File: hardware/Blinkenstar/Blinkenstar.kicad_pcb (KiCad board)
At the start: 2 copper layers, 84.4 x 82.8 mm, 21 parts, among them J1 AudioJack2_Ground, U2 ATtiny88-A, U3 EEPROM-I2CEIAJ

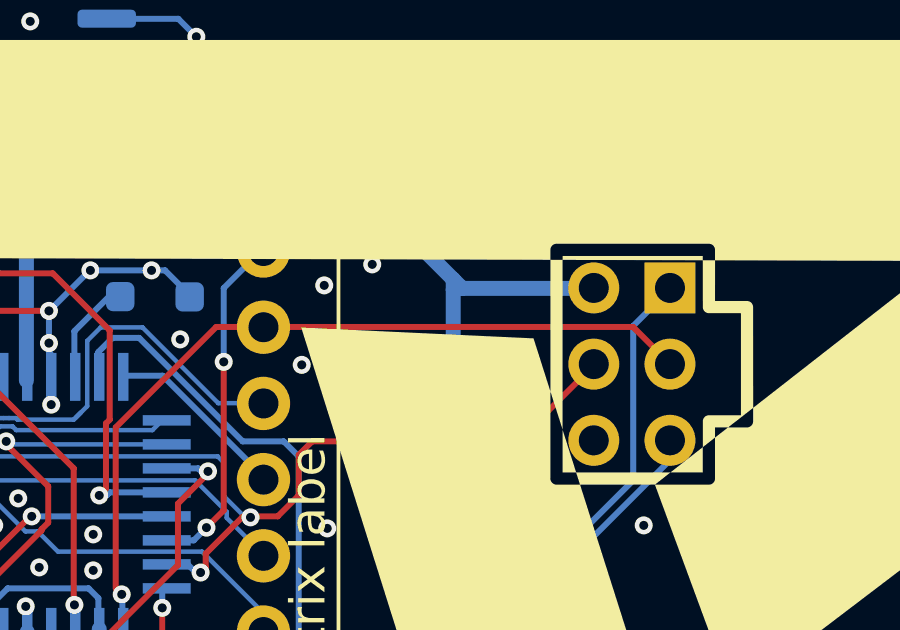
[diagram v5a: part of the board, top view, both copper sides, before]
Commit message: Adds CLKI connector for clock input
Adds a single-pin connector for external clock input (CLKI).

This enables the Blinkenstar to synchronize with an external clock source.

Also sets 'exclude_from_bom' and 'dnp' attributes to the test point components.
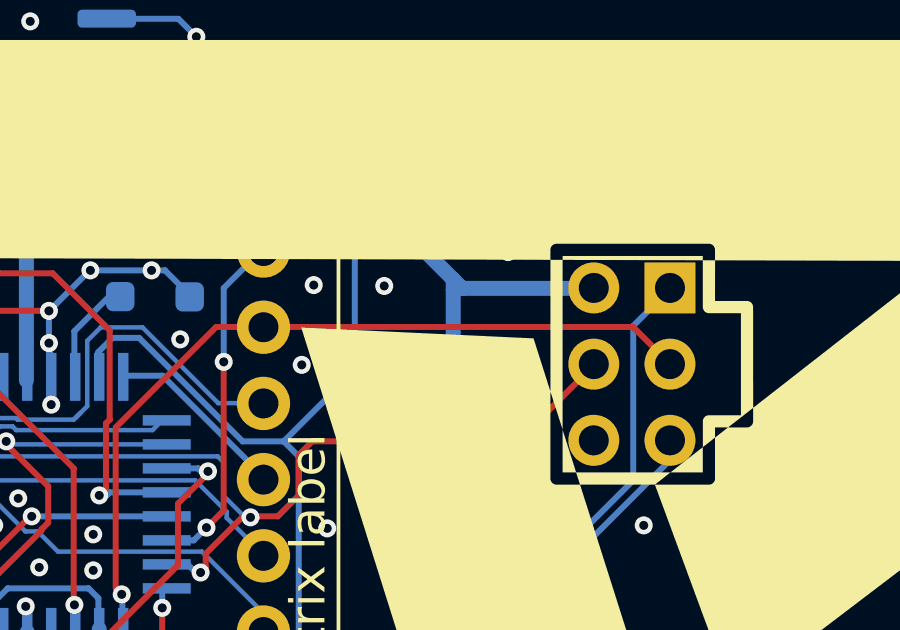
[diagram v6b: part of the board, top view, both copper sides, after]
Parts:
- added J3: CLKI, Connector_PinHeader_2.54mm:PinHeader_1x01_P2.54mm_Vertical, B.Cu at (133.4, 79.2)
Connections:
- net /R7 renamed /R7/CLKI
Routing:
- net /R7/CLKI: track 18.6 -> 35.0 mm, vias 0 -> 1
- net GND: vias 69 -> 70
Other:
- board text added: "CLKI +VCC MOSI GND"
- board text removed: "+VCC MOSI GND"
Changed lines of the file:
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@@
 	(net 6 "/C4")
 	(net 7 "/R2")
-	(net 8 "/R7")
+	(net 8 "/R7{slash}CLKI")
 	(net 9 "/C1")
 	(net 10 "/R3")
@@
 			(layers "*.Cu" "*.Mask")
 			(remove_unused_layers no)
-			(net 8 "/R7")
+			(net 8 "/R7{slash}CLKI")
 			(pinfunction "K7")
 			(pintype "bidirectional")
@@
 			(size 1.6 0.35)
 			(layers "B.Cu" "B.Mask" "B.Paste")
-			(net 8 "/R7")
+			(net 8 "/R7{slash}CLKI")
 			(pinfunction "PB6")
 			(pintype "bidirectional")
@@
 		(sheetname "/")
 		(sheetfile "Blinkenstar.kicad_sch")
-		(attr through_hole exclude_from_pos_files)
+		(attr through_hole exclude_from_pos_files exclude_from_bom dnp)
 		(fp_line
 			(start 3.87 1.33)
@@
 		)
 	)
+	(footprint "Connector_PinHeader_2.54mm:PinHeader_1x01_P2.54mm_Vertical"
+		(layer "B.Cu")
+		(at 133.385 79.225)
+		(descr "Through hole straight pin header, 1x01, 2.54mm pitch, single row")
+		(tags "Through hole pin header THT 1x01 2.54mm single row")
+		(property "Reference" "J3"
+			(at 0 2.38 180)
+			(layer "B.SilkS")
+			(effects
+				(font
+					(size 1 1)
+					(thickness 0.15)
+				)
+				(justify mirror)
+			)
+		)
+		(property "Value" "CLKI"
+			(at 0 -2.38 180)
+			(layer "B.Fab")
+			(effects
+				(font
+					(size 1 1)
+					(thickness 0.15)
+				)
+				(justify mirror)
+			)
+		)
+		(property "Datasheet" ""
+			(at 0 0 180)
+			(layer "B.Fab")
+			(hide yes)
+			(effects
+				(font
+					(size 1.27 1.27)
+					(thickness 0.15)
+				)
+				(justify mirror)
+			)
+		)
+		(property "Description" "Generic connector, single row, 01x01, script generated"
+			(at 0 0 180)
+			(layer "B.Fab")
+			(hide yes)
+			(effects
+				(font
+					(size 1.27 1.27)
+					(thickness 0.15)
+				)
+				(justify mirror)
+			)
+		)
+		(property ki_fp_filters "Connector*:*_1x??_*")
+		(sheetname "/")
+		(sheetfile "Blinkenstar.kicad_sch")
+		(attr through_hole exclude_from_pos_files exclude_from_bom dnp)
+		(fp_line
+			(start -1.77 -1.77)
+			(end 1.77 -1.77)
+			(stroke
+				(width 0.05)
+				(type solid)
+			)
+			(layer "B.CrtYd")
+		)
+		(fp_line
+			(start -1.77 1.77)
+			(end -1.77 -1.77)
+			(stroke
+				(width 0.05)
+				(type solid)
+			)
+			(layer "B.CrtYd")
+		)
+		(fp_line
+			(start 1.77 -1.77)
+			(end 1.77 1.77)
+			(stroke
+				(width 0.05)
+				(type solid)
+			)
+			(layer "B.CrtYd")
+		)
+		(fp_line
+			(start 1.77 1.77)
+			(end -1.77 1.77)
+			(stroke
+				(width 0.05)
+				(type solid)
+			)
+			(layer "B.CrtYd")
+		)
+		(fp_line
+			(start -1.27 -1.27)
+			(end -1.27 0.635)
+			(stroke
+				(width 0.1)
+				(type solid)
+			)
+			(layer "B.Fab")
+		)
+		(fp_line
+			(start -1.27 0.635)
+			(end -0.635 1.27)
+			(stroke
+				(width 0.1)
+				(type solid)
+			)
+			(layer "B.Fab")
+		)
+		(fp_line
+			(start -0.635 1.27)
+			(end 1.27 1.27)
+			(stroke
+				(width 0.1)
+				(type solid)
+			)
+			(layer "B.Fab")
+		)
+		(fp_line
+			(start 1.27 -1.27)
+			(end -1.27 -1.27)
+			(stroke
+				(width 0.1)
+				(type solid)
+			)
+			(layer "B.Fab")
+		)
+		(fp_line
+			(start 1.27 1.27)
+			(end 1.27 -1.27)
+			(stroke
+				(width 0.1)
+				(type solid)
+			)
+			(layer "B.Fab")
+		)
+		(fp_text user "${REFERENCE}"
+			(at 0 0 90)
+			(layer "B.Fab")
+			(effects
+				(font
+					(size 1 1)
+					(thickness 0.15)
+				)
+				(justify mirror)
+			)
+		)
+		(pad "1" thru_hole rect
+			(at 0 0)
+			(size 1.7 1.7)
+			(drill 1)
+			(layers "*.Cu" "*.Mask")
+			(remove_unused_layers no)
+			(net 8 "/R7{slash}CLKI")
+			(pinfunction "Pin_1")
+			(pintype "passive")
+		)
+		(embedded_fonts no)
+		(model "${KICAD9_3DMODEL_DIR}/Connector_PinHeader_2.54mm.3dshapes/PinHeader_1x01_P2.54mm_Vertical.step"
+			(offset
+				(xyz 0 0 0)
+			)
+			(scale
+				(xyz 1 1 1)
+			)
+			(rotate
+				(xyz 0 0 0)
+			)
+		)
+	)
 	(footprint "Resistor_SMD:R_0603_1608Metric_Pad0.98x0.95mm_HandSolder"
 		(layer "B.Cu")
@@
 	)
 	(gr_line
-		(start 131.1 79.05)
+		(start 131.699849 79.915)
 		(end 138 89)
 		(stroke
@@
 	)
 	(gr_line
-		(start 138.3 79)
+		(start 137.49 80.03)
 		(end 131.5 89)
 		(stroke
@@
 	)
 	(gr_text "ICSP"
-		(at 132.45 79.85 0)
+		(at 135.28 79.4 0)
 		(layer "B.SilkS")
 		(effects
@@
 		)
 	)
-	(gr_text "+VCC\nMOSI\nGND"
+	(gr_text "CLKI\n+VCC\nMOSI\nGND"
 		(at 131.65 87.9 0)
 		(layer "B.SilkS")
@@
 	)
 	(via
+		(at 130.53 80.59)
+		(size 0.6)
+		(drill 0.3)
+		(layers "F.Cu" "B.Cu")
+		(net 2)
+	)
+	(via
 		(at 120.6 100.7)
 		(size 0.6)
@@
 	)
 	(via
-		(at 126 81)
+		(at 126.4 81.72)
 		(size 0.6)
 		(drill 0.3)
@@
 	)
 	(via
-		(at 124.4 81.7)
+		(at 124.05 81.69)
 		(size 0.6)
 		(drill 0.3)
@@
 	)
 	(segment
+		(start 125.735 79.225)
+		(end 133.385 79.225)
+		(width 0.2)
+		(layer "F.Cu")
+		(net 8)
+	)
+	(segment
+		(start 125.42 79.54)
+		(end 125.735 79.225)
+		(width 0.2)
+		(layer "F.Cu")
+		(net 8)
+	)
+	(via
+		(at 125.42 79.54)
+		(size 0.6)
+		(drill 0.3)
+		(layers "F.Cu" "B.Cu")
+		(net 8)
+	)
+	(segment
 		(start 123.55 87.4)
 		(end 123.05 86.9)
@@
 	)
 	(segment
+		(start 125.42 84.53)
+		(end 125.42 79.54)
+		(width 0.2)
+		(layer "B.Cu")
+		(net 8)
+	)
+	(segment
 		(start 123.55 94.530514)
 		(end 123.55 87.4)
@@
 		(width 0.2)
 		(layer "B.Cu")
+		(net 8)
+	)
+	(segment
+		(start 123.05 86.9)
+		(end 125.42 84.53)
+		(width 0.2)
+		(layer "B.Cu")

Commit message: feat: add audio output and sine wave generation functionality
- Implemented audio output capabilities with the Speaker module.
- Created functions for generating and playing sine wave PCM audio.
- Added transfer tone encoding and playback features.
- Developed tests for audio output, sine wave generation, and transfer tone encoding.
- Ensured all scripts are in ES module format and removed legacy .js files.
- Updated package.json to include new test scripts for audio functionalities.
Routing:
- net /AVR_AUDIO_IN: track 28.1 -> 29.0 mm
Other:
- board text added: "v2.8"
- board text removed: "v2.7"

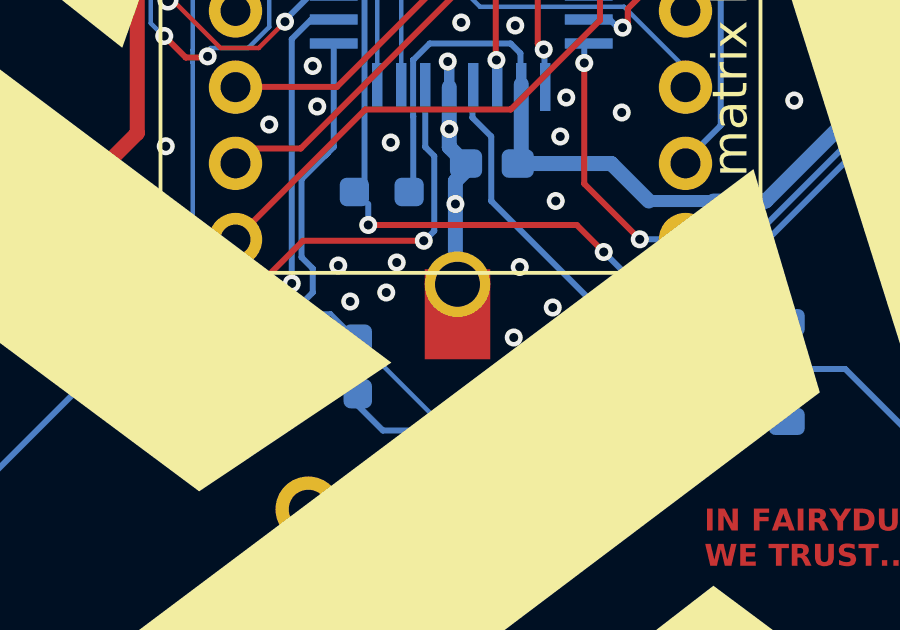
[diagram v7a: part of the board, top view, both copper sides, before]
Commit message: feat: Refine system interaction and modem reliability
- Invert stored pattern navigation button logic for improved user experience.
- Implement a two-button chord for waking from deep sleep, preventing accidental wake-ups.
- Ensure the FEC modem's state is cleared on initialization and report buffered decoded bytes immediately.
- Restart the modem receiver after ADC power is restored during system wake-up.
- Update KiCad project files and revise silkscreen elements for the latest hardware revision.
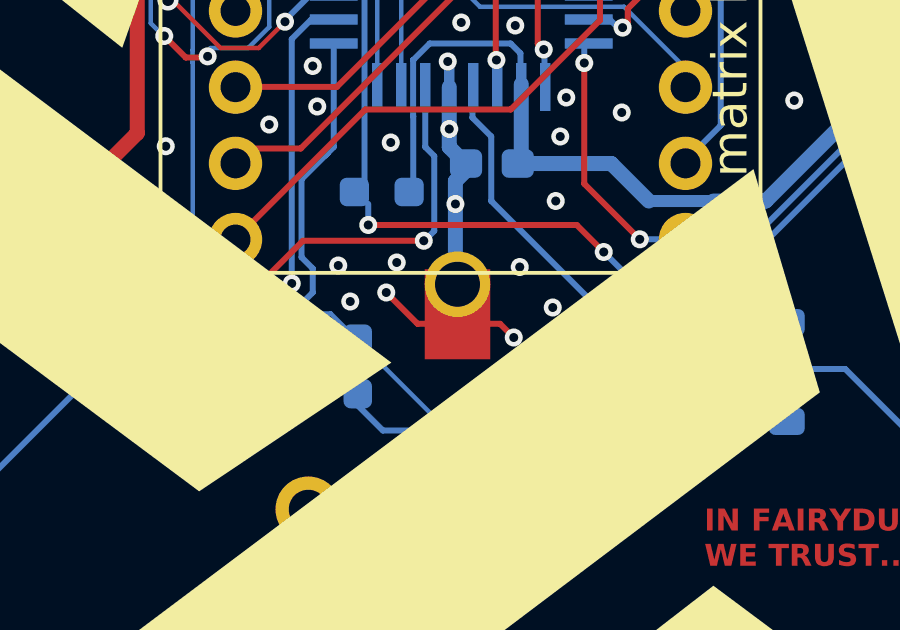
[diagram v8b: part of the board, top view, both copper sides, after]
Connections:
- J1 pad RING: (no net) -> Net-(J1-PadS)
- J1 pad SLEEVE: (no net) -> GND
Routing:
- net GND: track 29.4 -> 34.3 mm
